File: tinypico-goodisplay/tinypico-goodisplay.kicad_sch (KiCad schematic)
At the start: 23 parts, among them J1 AFC24-S24FIC-00, Q1 Si1308, U1 TinypicoESP32_Symbol

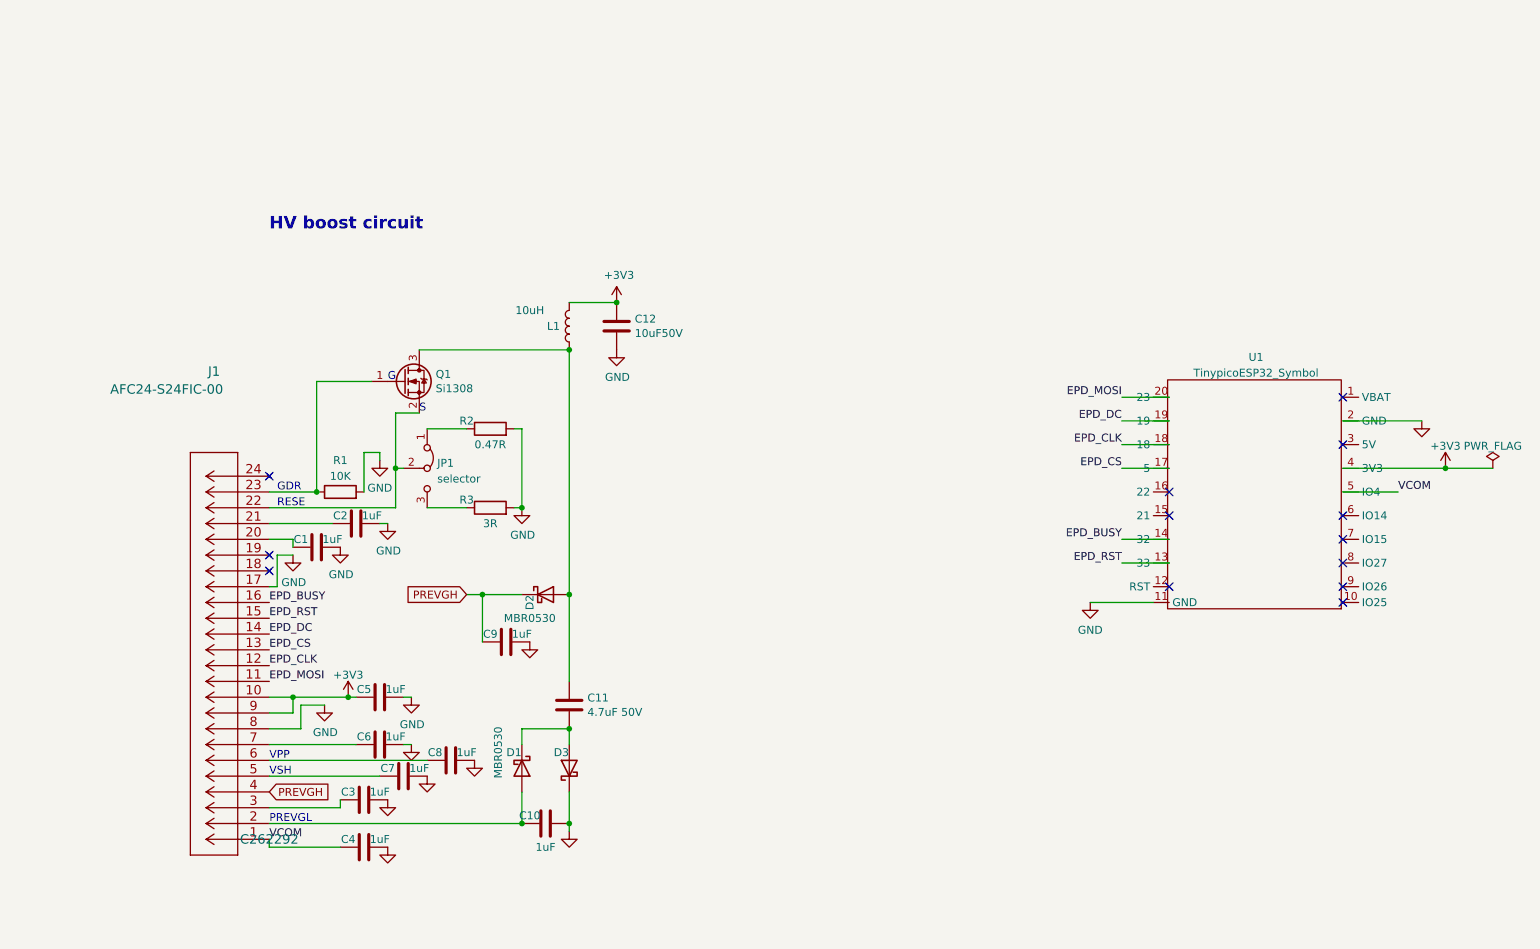
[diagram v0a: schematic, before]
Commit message: Add optional EPD_RST pullup to 3V3
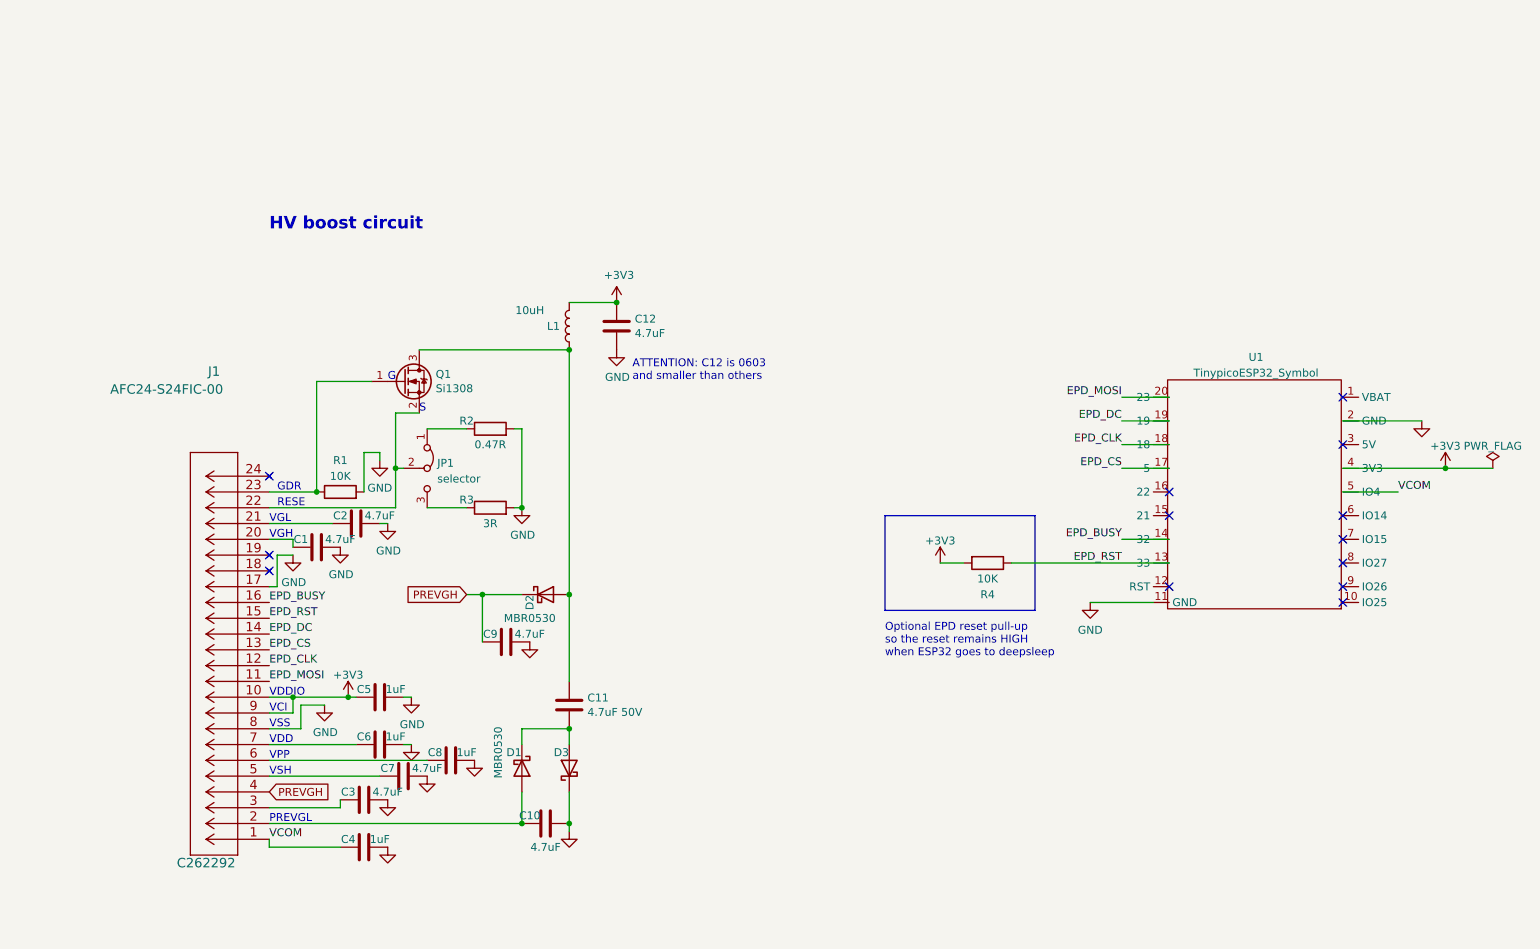
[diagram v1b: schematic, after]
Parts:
- added R4: 10K, Resistor_SMD:R_0603_1608Metric, symbol Device:R
- C1, C10, C2, C3, C7, C9: value 1uF -> 4.7uF; LCSC C28323 -> C1779
- C12: value 10uF50V -> 4.7uF; LCSC C96446 -> C19666
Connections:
- net +3V3: now also R4.2
- net EPD_RST: now also R4.1
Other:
- note added: "ATTENTION: C12 is 0603 and smaller than others"
- note added: "Optional EPD reset pull-up so the reset remains HIGH when ESP32 goes to deepsleep"
- note added: "VCI"
- note added: "VDD"
- note added: "VDDIO"
- note added: "VGH"
- note added: "VGL"
- note added: "VSS"

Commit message: #2 Add PCF8563 RTC
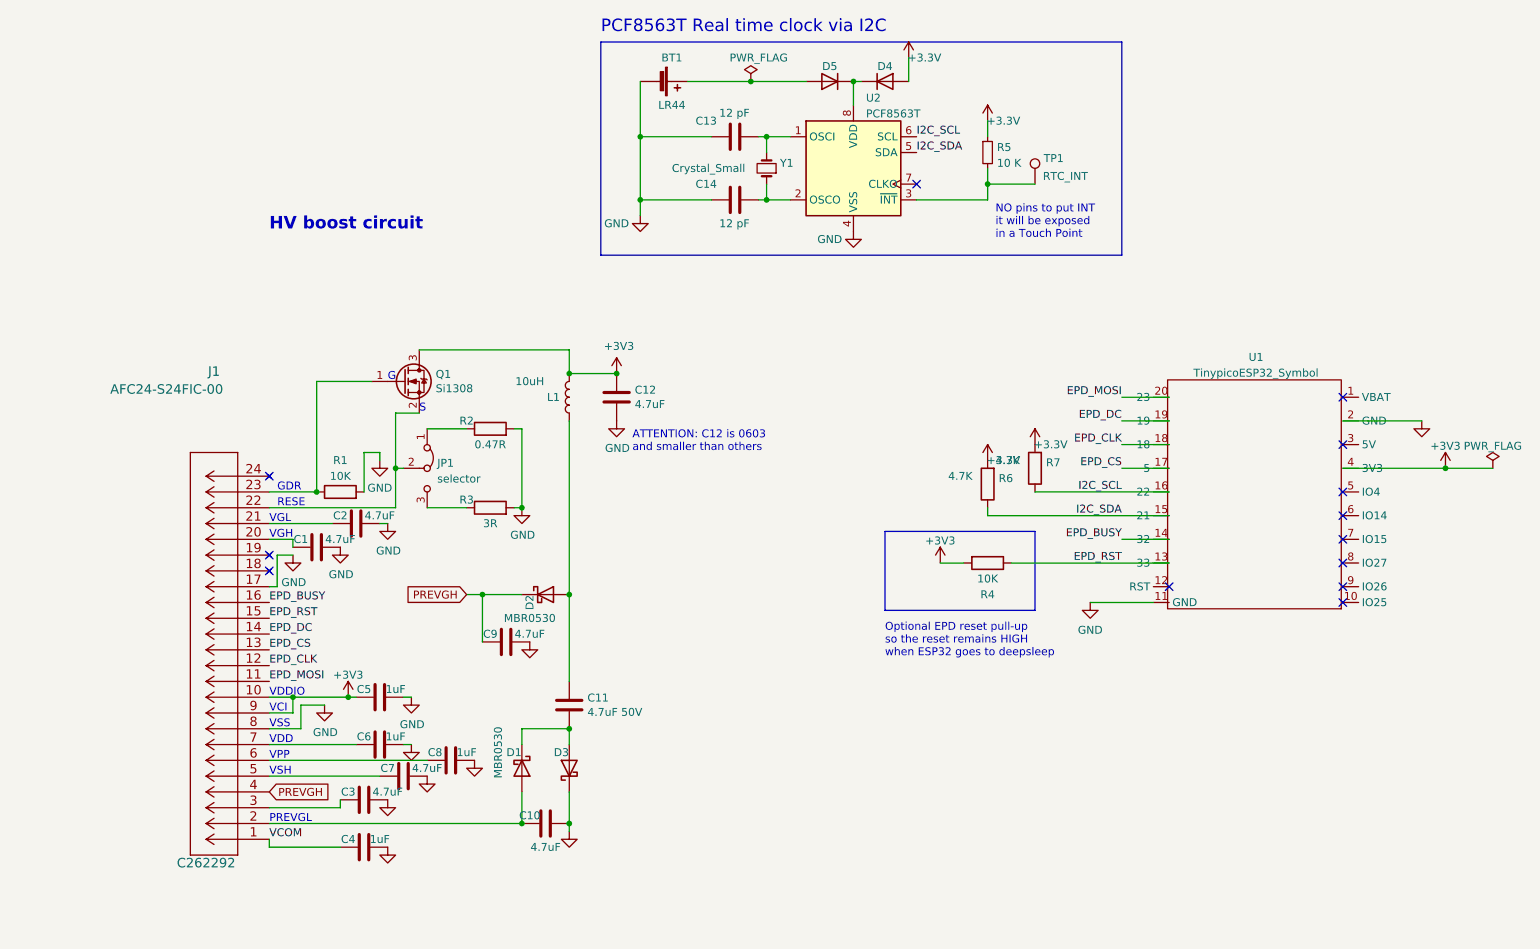
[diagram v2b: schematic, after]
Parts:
- added BT1: LR44, footprint:C964716_LR44, symbol Device:Battery_Cell
- added C13, C14: 12 pF, Capacitor_SMD:C_0603_1608Metric, symbol Device:C
- added D4, D5: 1N4148WS, Diode_SMD:D_SOD-323, symbol Diode:1N4148WS
- added R5: 10 K, Resistor_SMD:R_0603_1608Metric, symbol Device:R_Small
- added R6, R7: 4.7K, Resistor_SMD:R_0603_1608Metric, symbol Device:R
- added TP1: RTC_INT, TestPoint:TestPoint_Pad_D1.5mm, symbol Connector:TestPoint
- added U2: PCF8563T, Package_SO:SOIC-8_3.9x4.9mm_P1.27mm, symbol Timer_RTC:PCF8563T
- added Y1: Crystal_Small, footprint:Q13FC1350000400-Crystal, symbol Device:Crystal_Small
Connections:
- net +3V3: now also Q1.3 (D), D4.2 (A), R5.1, R6.2, R7.2
- net GND: now also BT1.2 (-), C13.1, C14.1, U2.4 (VSS)
- net VCOM: no longer U1.5 (IO4)
- net at C11.2, D2.2 (A), L1.1: no longer Q1.3 (D)
- net I2C_SDA: now reaches U1.15 (21)
- net I2C_SDA: now also R6.1, U2.5 (SDA)
- net I2C_SCL: now reaches U1.16 (22)
- net I2C_SCL: now also R7.1, U2.6 (SCL)
- new net: BT1.1 (+), D5.2 (A)
- new net: D4.1 (K), D5.1 (K), U2.8 (VDD)
- new net: R5.2, TP1.1, U2.3 (~{INT})
- new net: C14.2, U2.2 (OSCO), Y1.1
- new net: C13.2, U2.1 (OSCI), Y1.2
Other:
- note added: "NO pins to put INT it will be exposed in a Touch Point"
- note added: "PCF8563T Real time clock via I2C"
- moved on the sheet: C12, L1

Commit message: Correct routing, remove RTC TP1
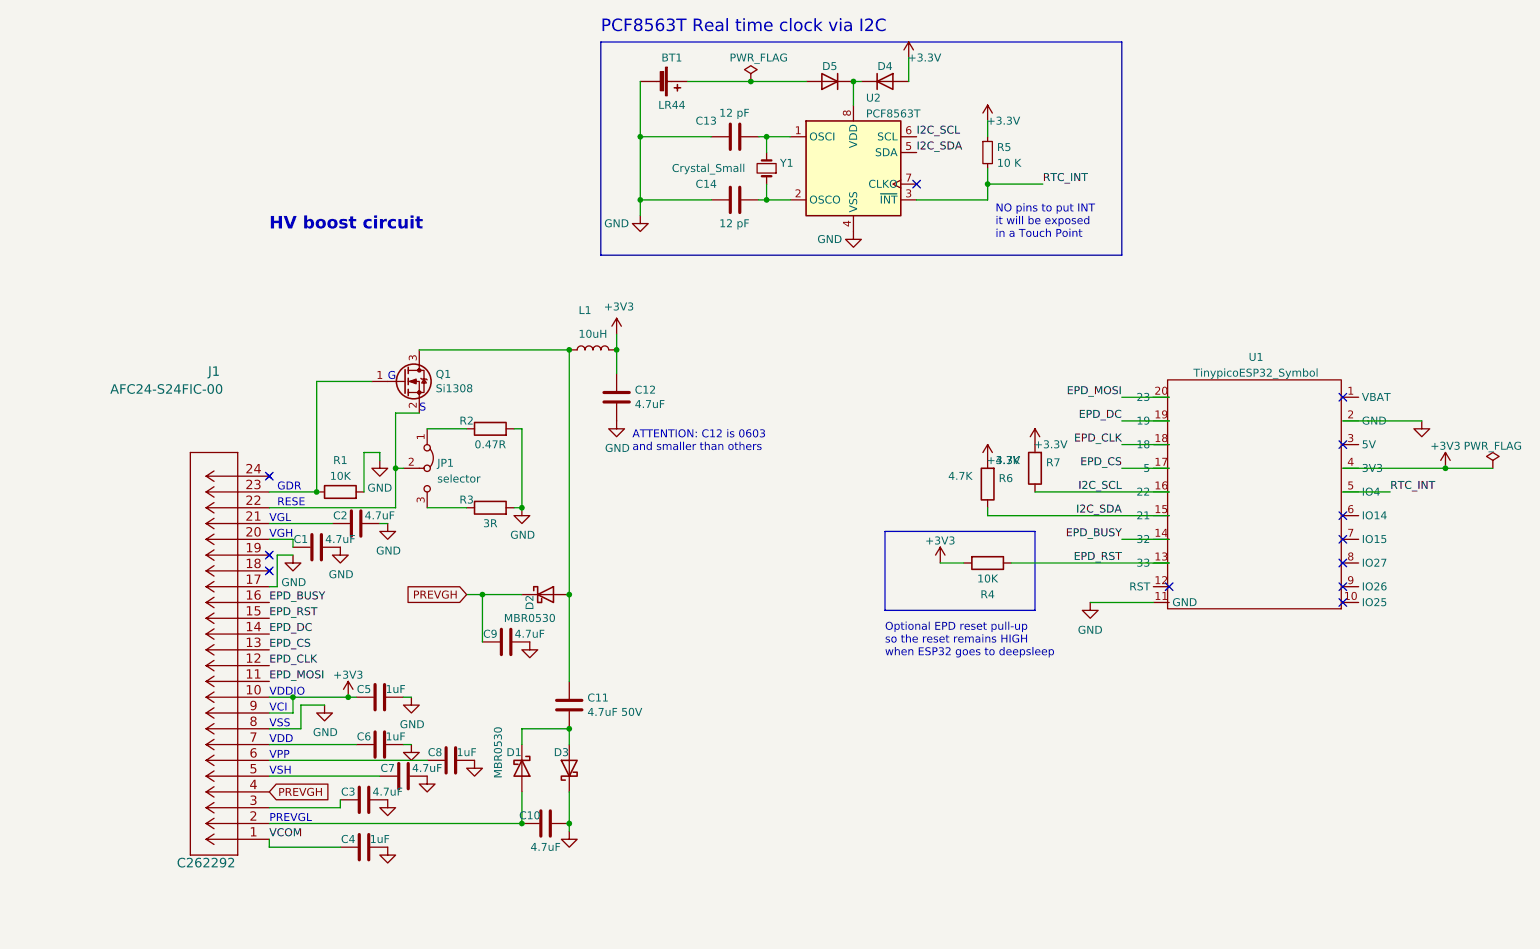
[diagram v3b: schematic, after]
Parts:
- removed TP1: RTC_INT, TestPoint:TestPoint_Pad_D1.5mm, symbol Connector:TestPoint
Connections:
- net +3V3: no longer Q1.3 (D)
- net at C11.2, D2.2 (A), L1.1: now also Q1.3 (D)
- net RTC_INT: now reaches R5.2, U2.3 (~{INT})
- net RTC_INT: now also U1.5 (IO4)
- no-connect marks 13 -> 12
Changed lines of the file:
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@@
   (junction (at 102.87 133.35) (diameter 0) (color 0 0 0 0)
   )
-  (junction (at 110.49 76.2) (diameter 0) (color 0 0 0 0)
-  )
   (junction (at 102.87 111.76) (diameter 0) (color 0 0 0 0)
   )
@@
   (junction (at 62.23 95.25) (diameter 0) (color 0 0 0 0)
   )
-  (junction (at 102.87 76.2) (diameter 0) (color 0 0 0 0)
-  )
   (junction (at 88.9 111.76) (diameter 0) (color 0 0 0 0)
   )
@@
   (junction (at 134.62 48.26) (diameter 0) (color 0 0 0 0)
   )
+  (junction (at 110.49 72.39) (diameter 0) (color 0 0 0 0)
+  )
   (junction (at 114.3 48.26) (diameter 0) (color 0 0 0 0)
+  )
+  (junction (at 102.87 72.39) (diameter 0) (color 0 0 0 0)
   )
   (no_connect (at 54.61 107.95))
@@
   (no_connect (at 54.61 105.41))
   (no_connect (at 227.33 87.63))
-  (no_connect (at 227.33 95.25))
   (no_connect (at 54.61 92.71))
   (no_connect (at 227.33 80.01))
@@
     (stroke (width 0) (type default) (color 0 0 0 0))
   )
-  (wire (pts (xy 102.87 83.82) (xy 102.87 111.76))
+  (wire (pts (xy 102.87 72.39) (xy 102.87 111.76))
     (stroke (width 0) (type default) (color 0 0 0 0))
   )
@@
     (stroke (width 0) (type default) (color 0 0 0 0))
   )
+  (wire (pts (xy 110.49 72.39) (xy 110.49 76.2))
+    (stroke (width 0) (type default) (color 0 0 0 0))
+  )
   (wire (pts (xy 148.59 29.21) (xy 149.86 29.21))
     (stroke (width 0) (type default) (color 0 0 0 0))
   )
-  (wire (pts (xy 170.18 45.72) (xy 177.8 45.72))
+  (wire (pts (xy 170.18 45.72) (xy 179.07 45.72))
     (stroke (width 0) (type default) (color 0 0 0 0))
   )
@@
     (stroke (width 0) (type default) (color 0 0 0 0))
   )
+  (wire (pts (xy 110.49 69.85) (xy 110.49 72.39))
+    (stroke (width 0) (type default) (color 0 0 0 0))
+  )
   (wire (pts (xy 54.61 146.05) (xy 66.04 146.05))
     (stroke (width 0) (type default) (color 0 0 0 0))
@@
     (stroke (width 0) (type default) (color 0 0 0 0))
   )
+  (wire (pts (xy 234.95 95.25) (xy 227.33 95.25))
+    (stroke (width 0) (type default) (color 0 0 0 0))
+  )
   (wire (pts (xy 86.36 97.79) (xy 80.01 97.79))
     (stroke (width 0) (type default) (color 0 0 0 0))
@@
     (stroke (width 0) (type default) (color 0 0 0 0))
   )
-  (wire (pts (xy 102.87 72.39) (xy 102.87 76.2))
-    (stroke (width 0) (type default) (color 0 0 0 0))
-  )
   (wire (pts (xy 102.87 149.86) (xy 102.87 148.59))
     (stroke (width 0) (type default) (color 0 0 0 0))
@@
   )
   (wire (pts (xy 191.77 91.44) (xy 199.39 91.44))
-    (stroke (width 0) (type default) (color 0 0 0 0))
-  )
-  (wire (pts (xy 102.87 76.2) (xy 110.49 76.2))
     (stroke (width 0) (type default) (color 0 0 0 0))
   )
@@
     (effects (font (size 1.27 1.27)) (justify left bottom))
   )
+  (label "RTC_INT" (at 234.95 95.25 0)
+    (effects (font (size 1.27 1.27)) (justify left bottom))
+  )
   (label "EPD_CLK" (at 54.61 123.19 0)
     (effects (font (size 1.27 1.27)) (justify left bottom))
@@
   (label "I2C_SCL" (at 191.77 95.25 180)
     (effects (font (size 1.27 1.27)) (justify right bottom))
+  )
+  (label "RTC_INT" (at 179.07 45.72 0)
+    (effects (font (size 1.27 1.27)) (justify left bottom))
   )
   (label "EPD_MOSI" (at 54.61 125.73 0)
@@
     )
   )
-  (symbol (lib_id "Device:L") (at 102.87 80.01 180) (unit 1)
-    (in_bom yes) (on_board yes)
-    (property "Reference" "L1" (id 0) (at 100.33 80.01 0))
-    (property "Value" "10uH" (id 1) (at 96.52 77.47 0))
-    (property "Footprint" "footprint:SWPA4030S1R0NT" (id 2) (at 102.87 80.01 0)
-      (effects (font (size 1.27 1.27)) hide)
-    )
-    (property "Datasheet" "https://jlcpcb.com/partdetail/Sunlord-SWPA4030S100MT/C38117" (id 3) (at 102.87 80.01 0)
-      (effects (font (size 1.27 1.27)) hide)
-    )
-    (property "LCSC" "C38117" (id 4) (at 102.87 80.01 0)
-      (effects (font (size 1.27 1.27)) hide)
-    )
-    (pin "1")
-    (pin "2")
-  )
   (symbol (lib_id "Device:C") (at 110.49 80.01 180) (unit 1)
     (in_bom yes) (on_board yes)
@@
     (pin "1")
   )
-  (symbol (lib_id "power:+3V3") (at 110.49 76.2 0) (unit 1)
-    (in_bom yes) (on_board yes)
-    (property "Reference" "#PWR0119" (id 0) (at 110.49 80.01 0)
-      (effects (font (size 1.27 1.27)) hide)
-    )
-    (property "Value" "+3V3" (id 1) (at 110.871 71.8058 0))
-    (property "Footprint" "" (id 2) (at 110.49 76.2 0)
-      (effects (font (size 1.27 1.27)) hide)
-    )
-    (property "Datasheet" "" (id 3) (at 110.49 76.2 0)
+  (symbol (lib_id "power:+3V3") (at 110.49 69.85 0) (unit 1)
+    (in_bom yes) (on_board yes)
+    (property "Reference" "#PWR0119" (id 0) (at 110.49 73.66 0)
+      (effects (font (size 1.27 1.27)) hide)
+    )
+    (property "Value" "+3V3" (id 1) (at 110.871 65.4558 0))
+    (property "Footprint" "" (id 2) (at 110.49 69.85 0)
+      (effects (font (size 1.27 1.27)) hide)
+    )
+    (property "Datasheet" "" (id 3) (at 110.49 69.85 0)
       (effects (font (size 1.27 1.27)) hide)
     )
@@
     (pin "2")
   )
+  (symbol (lib_id "Device:L") (at 106.68 72.39 90) (unit 1)
+    (in_bom yes) (on_board yes)
+    (property "Reference" "L1" (id 0) (at 105.41 66.04 90))
+    (property "Value" "10uH" (id 1) (at 106.68 69.85 90))
+    (property "Footprint" "footprint:SWPA4030S1R0NT" (id 2) (at 106.68 72.39 0)
+      (effects (font (size 1.27 1.27)) hide)
+    )
+    (property "Datasheet" "https://jlcpcb.com/partdetail/Sunlord-SWPA4030S100MT/C38117" (id 3) (at 106.68 72.39 0)
+      (effects (font (size 1.27 1.27)) hide)
+    )
+    (property "LCSC" "C38117" (id 4) (at 106.68 72.39 0)
+      (effects (font (size 1.27 1.27)) hide)
+    )
+    (pin "1")
+    (pin "2")
+  )
   (symbol (lib_id "power:GND") (at 148.59 53.34 0) (unit 1)
     (in_bom yes) (on_board yes)
@@
     (pin "1")
   )
-  (symbol (lib_id "Connector:TestPoint") (at 177.8 45.72 0) (unit 1)
-    (in_bom yes) (on_board yes)
-    (property "Reference" "TP1" (id 0) (at 179.197 41.5833 0)
-      (effects (font (size 1.27 1.27)) (justify left))
-    )
-    (property "Value" "RTC_INT" (id 1) (at 179.07 44.45 0)
-      (effects (font (size 1.27 1.27)) (justify left))
-    )
-    (property "Footprint" "TestPoint:TestPoint_Pad_D1.5mm" (id 2) (at 182.88 45.72 0)
-      (effects (font (size 1.27 1.27)) hide)
-    )
-    (property "Datasheet" "~" (id 3) (at 182.88 45.72 0)
-      (effects (font (size 1.27 1.27)) hide)
-    )
-    (pin "1")
-  )
   (symbol (lib_id "power:PWR_FLAG") (at 132.08 29.21 0) (unit 1)
     (in_bom yes) (on_board yes)
@@
       (reference "JP1") (unit 1) (value "selector") (footprint "footprint:switch-MK-12C02-G020")
     )
-    (path "/00000000-0000-0000-0000-0000606b755b"
+    (path "/24d70385-cad1-4002-8366-98d784569bfc"
       (reference "L1") (unit 1) (value "10uH") (footprint "footprint:SWPA4030S1R0NT")
     )
@@
       (reference "R7") (unit 1) (value "4.7K") (footprint "Resistor_SMD:R_0603_1608Metric")
     )
-    (path "/d99aa3fc-b5fc-4eee-91e4-8ee0ebd402ca"
-      (reference "TP1") (unit 1) (value "RTC_INT") (footprint "TestPoint:TestPoint_Pad_D1.5mm")
-    )
     (path "/b6a25dcd-a663-4d80-b0a5-a19a7ec28c71"
